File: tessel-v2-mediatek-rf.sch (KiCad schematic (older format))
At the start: 0 parts

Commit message: rf chain done (*starts praying*)
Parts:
- added AE? (x2): ANTENNA, symbol ANTENNA
- added AE? (x2): UFL, symbol UFL
- added C? (x4): 2.2pF, symbol C
- added C? (x4): 100pF, symbol C
- added C? (x2): 0.8pF, symbol C
- added C? (x4): 1.2pF, symbol C
- added C? (x4): 1.8pF, symbol C
- added L? (x4): 3nH, symbol INDUCTOR
- added L? (x4): 2.7nH, symbol INDUCTOR
- added L? (x2): 2.4nH, symbol INDUCTOR
- added R? (x2): 0R DNP, symbol R
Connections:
- net labels added: GND, RF0_BALUN_IN, RF0_CHIP_ANT, RF0_OUTN, RF0_OUTN_TCIN, RF0_OUTN_TCOUT, RF0_OUTP, RF0_OUTP_TCIN, RF0_OUTP_TCOUT, RF0_UFL, RF1_BALUN_IN, RF1_CHIP_ANT, RF1_OUTN, RF1_OUTN_TCIN, RF1_OUTN_TCOUT, RF1_OUTP, RF1_OUTP_TCIN, RF1_OUTP_TCOUT, RF1_UFL
- wire segments 0 -> 84

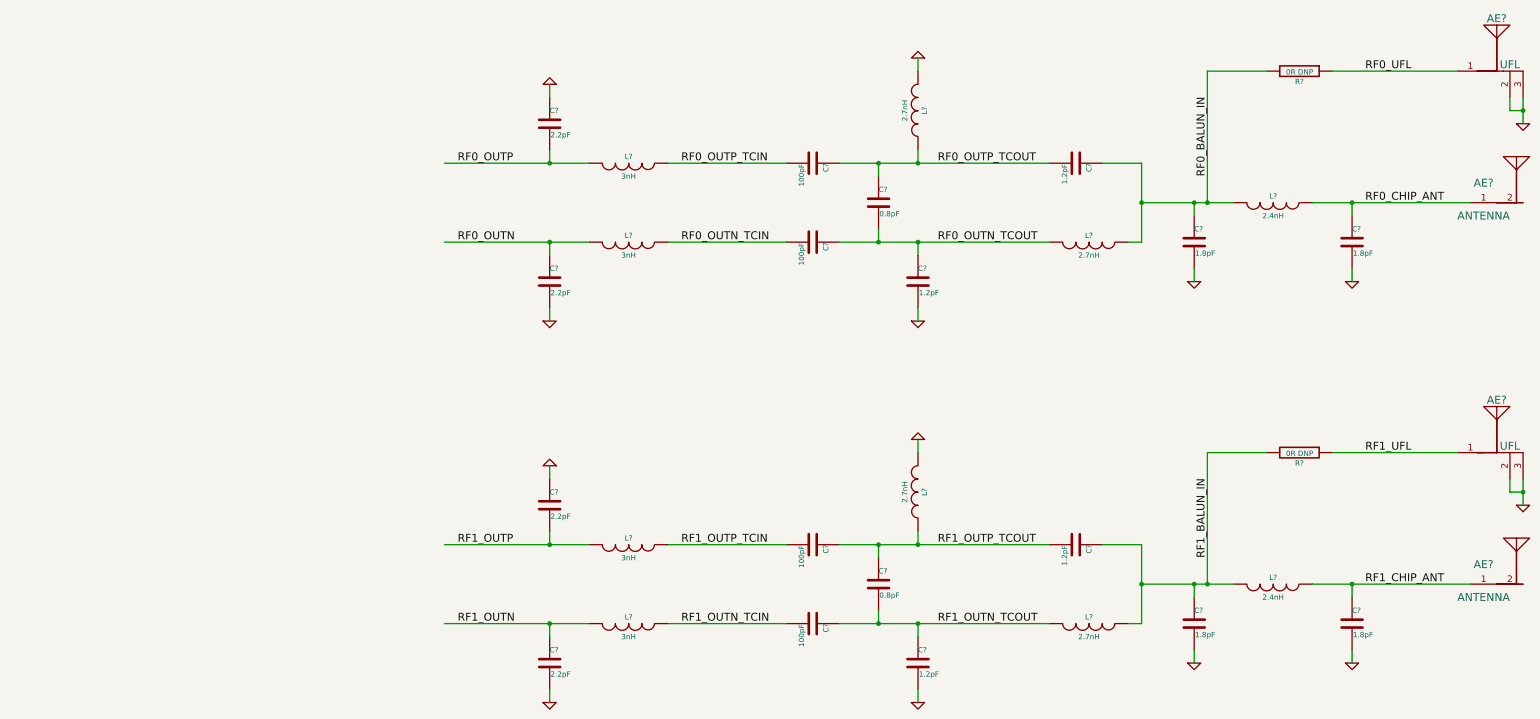
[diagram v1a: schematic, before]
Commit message: cleaning up ram, rf, and mediatek power
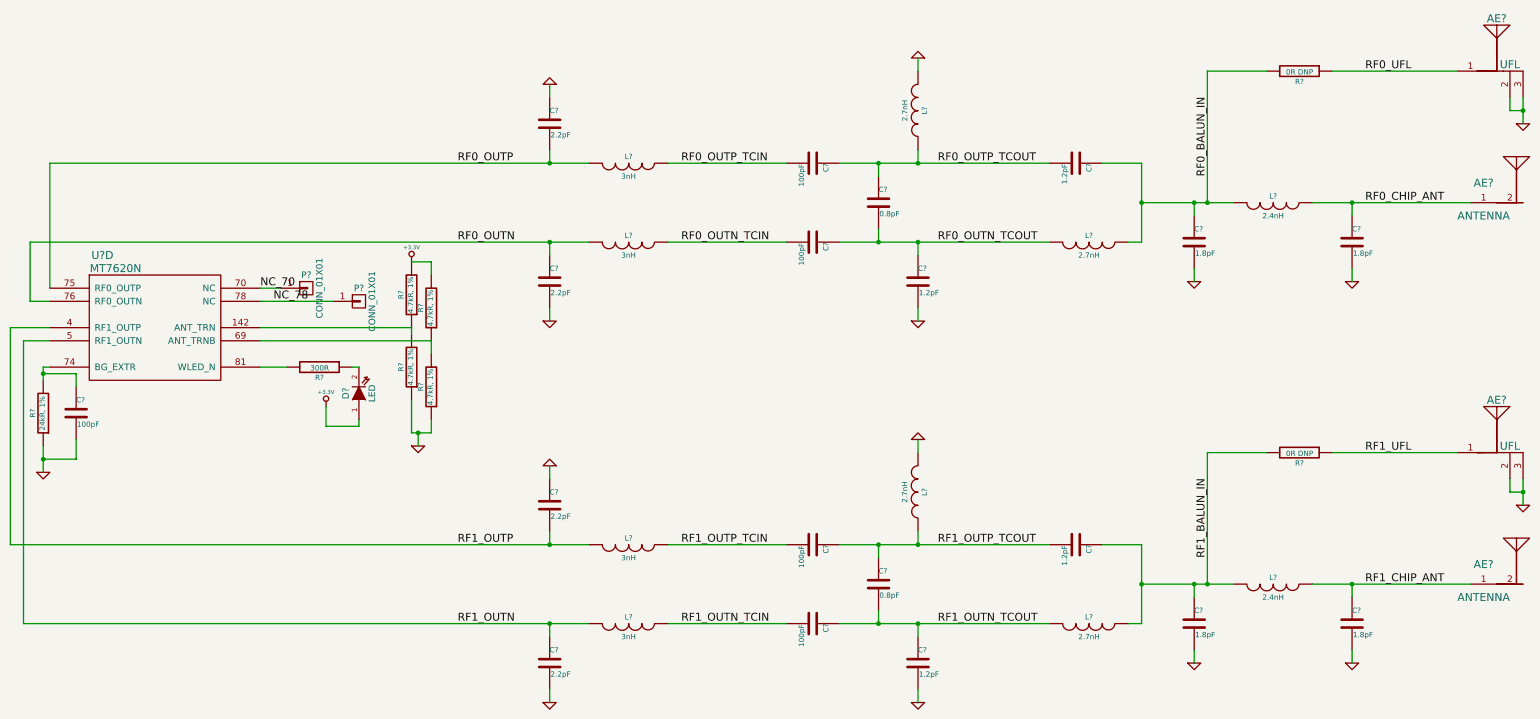
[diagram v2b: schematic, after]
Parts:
- added C?: 100pF, symbol C
- added D?: LED, symbol LED
- added P? (x2): CONN_01X01, symbol CONN_01X01
- added R?: 300R, symbol R
- added R?: 24kR, 1%, symbol R
- added R? (x4): 4.7kR, 1%, symbol R
- added U?: MT7620N, symbol MT7620N
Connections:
- net labels added: +3.3V, NC_70, NC_78
- wire segments 84 -> 93

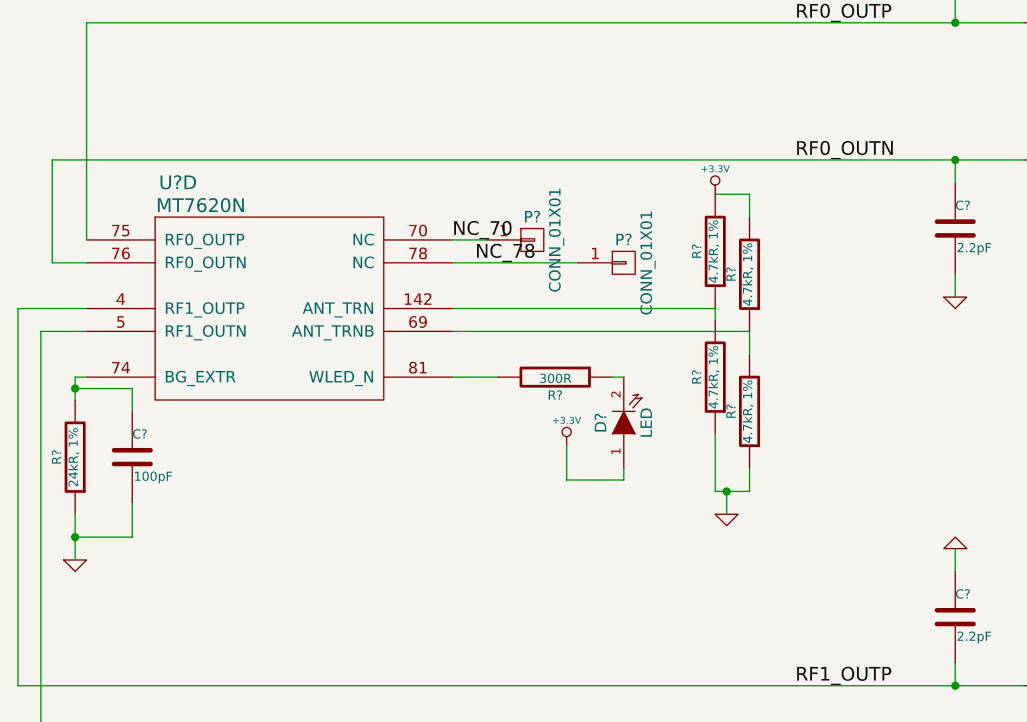
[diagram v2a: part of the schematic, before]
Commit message: setting default boot pins on rf
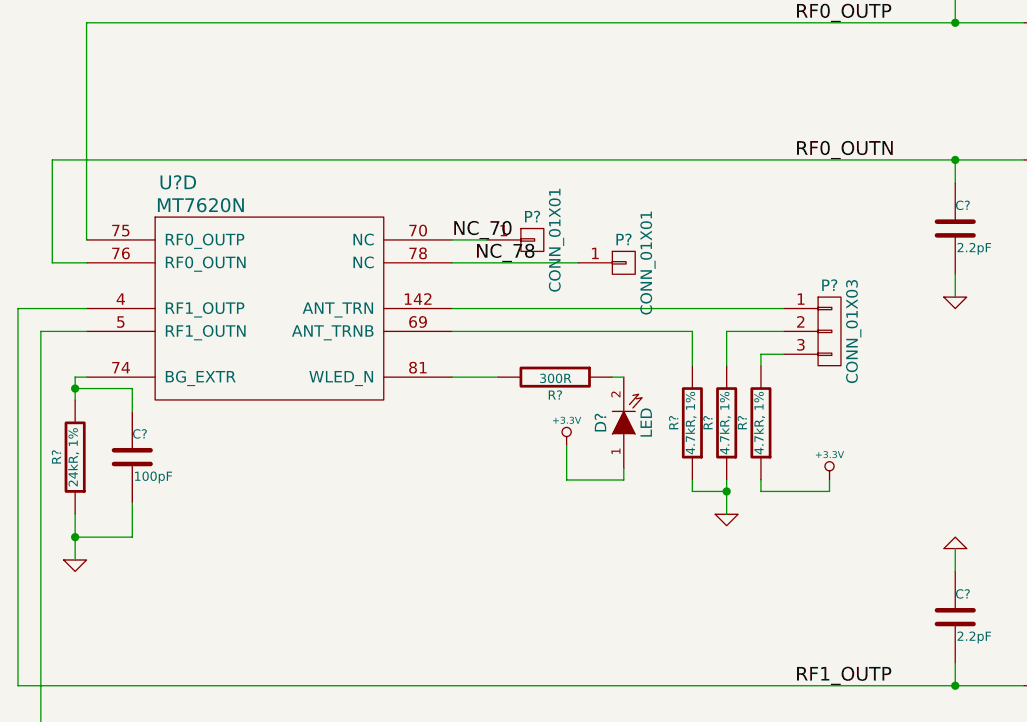
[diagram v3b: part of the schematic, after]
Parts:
- removed R?: 4.7kR, 1%, symbol R
- added P?: CONN_01X03, symbol CONN_01X03
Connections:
- net +3.3V: now also R?.1; no longer R?.2
- new net: P?.1 (P1), U?.142 (ANT_TRN)
- new net: P?.3 (P3), R?.2
- new net: P?.2 (P2), R?.2
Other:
- moved on the sheet: R?
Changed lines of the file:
@@
 	4450 5550 4450 5600
 Wire Wire Line
-	2050 5250 2050 5150
+	2050 5150 2050 5250
 Wire Wire Line
 	2050 5150 2100 5150
 Wire Wire Line
-	2050 5950 2050 5750
+	2050 5750 2050 5950
 Wire Wire Line
 	2300 5300 2300 5200
@@
 Wire Wire Line
 	4200 5600 4450 5600
-Wire Wire Line
-	3700 4850 4850 4850
 $Comp
 L R R?
 U 1 1 5491920E
-P 4850 4600
-F 0 "R?" V 4930 4600 40  0000 C CNN
-F 1 "4.7kR, 1%" V 4857 4601 40  0000 C CNN
-F 2 "" V 4780 4600 30  0000 C CNN
-F 3 "" H 4850 4600 30  0000 C CNN
-	1    4850 4600
+P 5050 5350
+F 0 "R?" V 5130 5350 40  0000 C CNN
+F 1 "4.7kR, 1%" V 5057 5351 40  0000 C CNN
+F 2 "" V 4980 5350 30  0000 C CNN
+F 3 "" H 5050 5350 30  0000 C CNN
+	1    5050 5350
 	-1   0    0    1
 $EndComp
@@
 L +3.3V #PWR?
 U 1 1 54919282
-P 4850 4350
-F 0 "#PWR?" H 4850 4310 30  0001 C CNN
-F 1 "+3.3V" H 4850 4460 30  0000 C CNN
-F 2 "" H 4850 4350 60  0000 C CNN
-F 3 "" H 4850 4350 60  0000 C CNN
-	1    4850 4350
+P 5350 5600
+F 0 "#PWR?" H 5350 5560 30  0001 C CNN
+F 1 "+3.3V" H 5350 5710 30  0000 C CNN
+F 2 "" H 5350 5600 60  0000 C CNN
+F 3 "" H 5350 5600 60  0000 C CNN
+	1    5350 5600
 	1    0    0    -1
 $EndComp
@@
 L R R?
 U 1 1 5491938E
-P 4850 5150
-F 0 "R?" V 4930 5150 40  0000 C CNN
-F 1 "4.7kR, 1%" V 4857 5151 40  0000 C CNN
-F 2 "" V 4780 5150 30  0000 C CNN
-F 3 "" H 4850 5150 30  0000 C CNN
-	1    4850 5150
+P 4900 5350
+F 0 "R?" V 4980 5350 40  0000 C CNN
+F 1 "4.7kR, 1%" V 4907 5351 40  0000 C CNN
+F 2 "" V 4830 5350 30  0000 C CNN
+F 3 "" H 4900 5350 30  0000 C CNN
+	1    4900 5350
 	-1   0    0    1
 $EndComp
@@
 L R R?
 U 1 1 54919448
-P 5000 5300
-F 0 "R?" V 5080 5300 40  0000 C CNN
-F 1 "4.7kR, 1%" V 5007 5301 40  0000 C CNN
-F 2 "" V 4930 5300 30  0000 C CNN
-F 3 "" H 5000 5300 30  0000 C CNN
-	1    5000 5300
-	-1   0    0    1
-$EndComp
-$Comp
-L R R?
-U 1 1 54919496
-P 5000 4700
-F 0 "R?" V 5080 4700 40  0000 C CNN
-F 1 "4.7kR, 1%" V 5007 4701 40  0000 C CNN
-F 2 "" V 4930 4700 30  0000 C CNN
-F 3 "" H 5000 4700 30  0000 C CNN
-	1    5000 4700
+P 4750 5350
+F 0 "R?" V 4830 5350 40  0000 C CNN
+F 1 "4.7kR, 1%" V 4757 5351 40  0000 C CNN
+F 2 "" V 4680 5350 30  0000 C CNN
+F 3 "" H 4750 5350 30  0000 C CNN
+	1    4750 5350
 	-1   0    0    1
 $EndComp
 Wire Wire Line
-	3700 4950 5000 4950
+	3700 4950 4750 4950
 Wire Wire Line
-	4850 4850 4850 4900
+	4750 4950 4750 5100
 Wire Wire Line
-	5000 4950 5000 5050
+	4750 5650 4750 5600
 Wire Wire Line
-	4850 5400 4850 5650
+	4900 5600 4900 5750
+Connection ~ 4900 5650
+$Comp
+L CONN_01X03 P?
+U 1 1 5491EAD6
+P 5350 4950
+F 0 "P?" H 5350 5150 50  0000 C CNN
+F 1 "CONN_01X03" V 5450 4950 50  0000 C CNN
+F 2 "" H 5350 4950 60  0000 C CNN
+F 3 "" H 5350 4950 60  0000 C CNN
+	1    5350 4950
+	1    0    0    -1
+$EndComp
 Wire Wire Line
-	4850 5650 5000 5650
+	3700 4850 5150 4850
 Wire Wire Line
-	5000 5650 5000 5550
+	5150 4950 4900 4950
 Wire Wire Line
-	4900 5650 4900 5750
-Connection ~ 4900 5650
+	4900 4950 4900 5100
 Wire Wire Line
-	5000 4450 5000 4350
+	4900 5650 4750 5650
 Wire Wire Line
-	5000 4350 4850 4350
+	5050 5600 5050 5650
+Wire Wire Line
+	5050 5650 5350 5650
+Wire Wire Line
+	5350 5650 5350 5600
+Wire Wire Line
+	5050 5100 5050 5050
+Wire Wire Line
+	5050 5050 5150 5050
 $EndSCHEMATC

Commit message: annotated
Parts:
- gave numbers to parts that had none: 45

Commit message: second pass schem check
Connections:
- net at U201.142 (ANT_TRN): now also P503.2 (P2); no longer P503.1 (P1)
- net at R504.2: now also P503.1 (P1); no longer P503.2 (P2)
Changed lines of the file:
@@
 $EndComp
 Wire Wire Line
-	3700 4850 5150 4850
-Wire Wire Line
-	5150 4950 4900 4950
-Wire Wire Line
-	4900 4950 4900 5100
+	4900 4900 4900 5100
 Wire Wire Line
 	4900 5650 4750 5650
@@
 Wire Wire Line
 	5050 5050 5150 5050
+Wire Wire Line
+	3700 4850 5000 4850
+Wire Wire Line
+	5000 4850 5000 4950
+Wire Wire Line
+	5000 4950 5150 4950
+Wire Wire Line
+	4900 4900 5050 4900
+Wire Wire Line
+	5050 4900 5050 4850
+Wire Wire Line
+	5050 4850 5150 4850
 $EndSCHEMATC

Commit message: adding netlist, checked for single-pin nets
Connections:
- no-connect marks 0 -> 2
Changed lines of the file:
@@
 $EndComp
 $Comp
-L GND #PWR513
+L GND #PWR027
 U 1 1 5492119C
 P 10800 4500
-F 0 "#PWR513" H 10800 4500 30  0001 C CNN
+F 0 "#PWR027" H 10800 4500 30  0001 C CNN
 F 1 "GND" H 10800 4430 30  0001 C CNN
 F 2 "" H 10800 4500 60  0000 C CNN
@@
 $EndComp
 $Comp
-L GND #PWR515
+L GND #PWR028
 U 1 1 549211F2
 P 12000 4500
-F 0 "#PWR515" H 12000 4500 30  0001 C CNN
+F 0 "#PWR028" H 12000 4500 30  0001 C CNN
 F 1 "GND" H 12000 4430 30  0001 C CNN
 F 2 "" H 12000 4500 60  0000 C CNN
@@
 $EndComp
 $Comp
-L GND #PWR517
+L GND #PWR029
 U 1 1 54921339
 P 13300 3300
-F 0 "#PWR517" H 13300 3300 30  0001 C CNN
+F 0 "#PWR029" H 13300 3300 30  0001 C CNN
 F 1 "GND" H 13300 3230 30  0001 C CNN
 F 2 "" H 13300 3300 60  0000 C CNN
@@
 $EndComp
 $Comp
-L GND #PWR510
+L GND #PWR030
 U 1 1 54921901
 P 8700 4800
-F 0 "#PWR510" H 8700 4800 30  0001 C CNN
+F 0 "#PWR030" H 8700 4800 30  0001 C CNN
 F 1 "GND" H 8700 4730 30  0001 C CNN
 F 2 "" H 8700 4800 60  0000 C CNN
@@
 $EndComp
 $Comp
-L GND #PWR506
+L GND #PWR031
 U 1 1 54921B0A
 P 5900 4800
-F 0 "#PWR506" H 5900 4800 30  0001 C CNN
+F 0 "#PWR031" H 5900 4800 30  0001 C CNN
 F 1 "GND" H 5900 4730 30  0001 C CNN
 F 2 "" H 5900 4800 60  0000 C CNN
@@
 $EndComp
 $Comp
-L GND #PWR505
+L GND #PWR032
 U 1 1 54921B48
 P 5900 3000
-F 0 "#PWR505" H 5900 3000 30  0001 C CNN
+F 0 "#PWR032" H 5900 3000 30  0001 C CNN
 F 1 "GND" H 5900 2930 30  0001 C CNN
 F 2 "" H 5900 3000 60  0000 C CNN
@@
 $EndComp
 $Comp
-L GND #PWR509
+L GND #PWR033
 U 1 1 54921BCA
 P 8700 2800
-F 0 "#PWR509" H 8700 2800 30  0001 C CNN
+F 0 "#PWR033" H 8700 2800 30  0001 C CNN
 F 1 "GND" H 8700 2730 30  0001 C CNN
 F 2 "" H 8700 2800 60  0000 C CNN
@@
 $EndComp
 $Comp
-L GND #PWR514
+L GND #PWR034
 U 1 1 5492F3B9
 P 10800 7400
-F 0 "#PWR514" H 10800 7400 30  0001 C CNN
+F 0 "#PWR034" H 10800 7400 30  0001 C CNN
 F 1 "GND" H 10800 7330 30  0001 C CNN
 F 2 "" H 10800 7400 60  0000 C CNN
@@
 $EndComp
 $Comp
-L GND #PWR516
+L GND #PWR035
 U 1 1 5492F3BF
 P 12000 7400
-F 0 "#PWR516" H 12000 7400 30  0001 C CNN
+F 0 "#PWR035" H 12000 7400 30  0001 C CNN
 F 1 "GND" H 12000 7330 30  0001 C CNN
 F 2 "" H 12000 7400 60  0000 C CNN
@@
 $EndComp
 $Comp
-L GND #PWR518
+L GND #PWR036
 U 1 1 5492F3C5
 P 13300 6200
-F 0 "#PWR518" H 13300 6200 30  0001 C CNN
+F 0 "#PWR036" H 13300 6200 30  0001 C CNN
 F 1 "GND" H 13300 6130 30  0001 C CNN
 F 2 "" H 13300 6200 60  0000 C CNN
@@
 $EndComp
 $Comp
-L GND #PWR512
+L GND #PWR037
 U 1 1 5492F3D0
 P 8700 7700
-F 0 "#PWR512" H 8700 7700 30  0001 C CNN
+F 0 "#PWR037" H 8700 7700 30  0001 C CNN
 F 1 "GND" H 8700 7630 30  0001 C CNN
 F 2 "" H 8700 7700 60  0000 C CNN
@@
 $EndComp
 $Comp
-L GND #PWR508
+L GND #PWR038
 U 1 1 5492F3D6
 P 5900 7700
-F 0 "#PWR508" H 5900 7700 30  0001 C CNN
+F 0 "#PWR038" H 5900 7700 30  0001 C CNN
 F 1 "GND" H 5900 7630 30  0001 C CNN
 F 2 "" H 5900 7700 60  0000 C CNN
@@
 $EndComp
 $Comp
-L GND #PWR507
+L GND #PWR039
 U 1 1 5492F3DC
 P 5900 5900
-F 0 "#PWR507" H 5900 5900 30  0001 C CNN
+F 0 "#PWR039" H 5900 5900 30  0001 C CNN
 F 1 "GND" H 5900 5830 30  0001 C CNN
 F 2 "" H 5900 5900 60  0000 C CNN
@@
 $EndComp
 $Comp
-L GND #PWR511
+L GND #PWR040
 U 1 1 5492F3E2
 P 8700 5700
-F 0 "#PWR511" H 8700 5700 30  0001 C CNN
+F 0 "#PWR040" H 8700 5700 30  0001 C CNN
 F 1 "GND" H 8700 5630 30  0001 C CNN
 F 2 "" H 8700 5700 60  0000 C CNN
@@
 $EndComp
 $Comp
-L +3.3V #PWR502
+L +3.3V #PWR041
 U 1 1 54916FFB
 P 4200 5450
-F 0 "#PWR502" H 4200 5410 30  0001 C CNN
+F 0 "#PWR041" H 4200 5410 30  0001 C CNN
 F 1 "+3.3V" H 4200 5560 30  0000 C CNN
 F 2 "" H 4200 5450 60  0000 C CNN
@@
 $EndComp
 $Comp
-L GND #PWR501
+L GND #PWR042
 U 1 1 54917BEF
 P 2050 5950
-F 0 "#PWR501" H 2050 5950 30  0001 C CNN
+F 0 "#PWR042" H 2050 5950 30  0001 C CNN
 F 1 "GND" H 2050 5880 30  0001 C CNN
 F 2 "" H 2050 5950 60  0000 C CNN
@@
 NC_78
 $Comp
-L GND #PWR503
+L GND #PWR043
 U 1 1 54918F7B
 P 4900 5750
-F 0 "#PWR503" H 4900 5750 30  0001 C CNN
+F 0 "#PWR043" H 4900 5750 30  0001 C CNN
 F 1 "GND" H 4900 5680 30  0001 C CNN
 F 2 "" H 4900 5750 60  0000 C CNN
@@
 $EndComp
 $Comp
-L +3.3V #PWR504
+L +3.3V #PWR044
 U 1 1 54919282
 P 5350 5600
-F 0 "#PWR504" H 5350 5560 30  0001 C CNN
+F 0 "#PWR044" H 5350 5560 30  0001 C CNN
 F 1 "+3.3V" H 5350 5710 30  0000 C CNN
 F 2 "" H 5350 5600 60  0000 C CNN
@@
 Wire Wire Line
 	5050 4850 5150 4850
+NoConn ~ 13300 3900
+NoConn ~ 13300 6800
 $EndSCHEMATC

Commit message: TIL: -am...but also P-->J
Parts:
- renumbered P501 to J501, P502 to J502, P503 to J503
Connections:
- net ANT_TRN: now reaches J503.2 (P2), U201.142 (ANT_TRN)
- net ANT_TRNB: now reaches R503.2, U201.69 (ANT_TRNB)
- net WLED_N: now reaches R502.2, U201.81 (WLED_N)
- net WLED_N_R: now reaches D501.2 (K), R502.1
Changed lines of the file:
@@
 $EndComp
 $Comp
-L GND #PWR027
+L GND #PWR513
 U 1 1 5492119C
 P 10800 4500
-F 0 "#PWR027" H 10800 4500 30  0001 C CNN
+F 0 "#PWR513" H 10800 4500 30  0001 C CNN
 F 1 "GND" H 10800 4430 30  0001 C CNN
 F 2 "" H 10800 4500 60  0000 C CNN
@@
 $EndComp
 $Comp
-L GND #PWR028
+L GND #PWR515
 U 1 1 549211F2
 P 12000 4500
-F 0 "#PWR028" H 12000 4500 30  0001 C CNN
+F 0 "#PWR515" H 12000 4500 30  0001 C CNN
 F 1 "GND" H 12000 4430 30  0001 C CNN
 F 2 "" H 12000 4500 60  0000 C CNN
@@
 $EndComp
 $Comp
-L GND #PWR029
+L GND #PWR517
 U 1 1 54921339
 P 13300 3300
-F 0 "#PWR029" H 13300 3300 30  0001 C CNN
+F 0 "#PWR517" H 13300 3300 30  0001 C CNN
 F 1 "GND" H 13300 3230 30  0001 C CNN
 F 2 "" H 13300 3300 60  0000 C CNN
@@
 $EndComp
 $Comp
-L GND #PWR030
+L GND #PWR510
 U 1 1 54921901
 P 8700 4800
-F 0 "#PWR030" H 8700 4800 30  0001 C CNN
+F 0 "#PWR510" H 8700 4800 30  0001 C CNN
 F 1 "GND" H 8700 4730 30  0001 C CNN
 F 2 "" H 8700 4800 60  0000 C CNN
@@
 $EndComp
 $Comp
-L GND #PWR031
+L GND #PWR506
 U 1 1 54921B0A
 P 5900 4800
-F 0 "#PWR031" H 5900 4800 30  0001 C CNN
+F 0 "#PWR506" H 5900 4800 30  0001 C CNN
 F 1 "GND" H 5900 4730 30  0001 C CNN
 F 2 "" H 5900 4800 60  0000 C CNN
@@
 $EndComp
 $Comp
-L GND #PWR032
+L GND #PWR505
 U 1 1 54921B48
 P 5900 3000
-F 0 "#PWR032" H 5900 3000 30  0001 C CNN
+F 0 "#PWR505" H 5900 3000 30  0001 C CNN
 F 1 "GND" H 5900 2930 30  0001 C CNN
 F 2 "" H 5900 3000 60  0000 C CNN
@@
 $EndComp
 $Comp
-L GND #PWR033
+L GND #PWR509
 U 1 1 54921BCA
 P 8700 2800
-F 0 "#PWR033" H 8700 2800 30  0001 C CNN
+F 0 "#PWR509" H 8700 2800 30  0001 C CNN
 F 1 "GND" H 8700 2730 30  0001 C CNN
 F 2 "" H 8700 2800 60  0000 C CNN
@@
 $EndComp
 $Comp
-L GND #PWR034
+L GND #PWR514
 U 1 1 5492F3B9
 P 10800 7400
-F 0 "#PWR034" H 10800 7400 30  0001 C CNN
+F 0 "#PWR514" H 10800 7400 30  0001 C CNN
 F 1 "GND" H 10800 7330 30  0001 C CNN
 F 2 "" H 10800 7400 60  0000 C CNN
@@
 $EndComp
 $Comp
-L GND #PWR035
+L GND #PWR516
 U 1 1 5492F3BF
 P 12000 7400
-F 0 "#PWR035" H 12000 7400 30  0001 C CNN
+F 0 "#PWR516" H 12000 7400 30  0001 C CNN
 F 1 "GND" H 12000 7330 30  0001 C CNN
 F 2 "" H 12000 7400 60  0000 C CNN
@@
 $EndComp
 $Comp
-L GND #PWR036
+L GND #PWR518
 U 1 1 5492F3C5
 P 13300 6200
-F 0 "#PWR036" H 13300 6200 30  0001 C CNN
+F 0 "#PWR518" H 13300 6200 30  0001 C CNN
 F 1 "GND" H 13300 6130 30  0001 C CNN
 F 2 "" H 13300 6200 60  0000 C CNN
@@
 $EndComp
 $Comp
-L GND #PWR037
+L GND #PWR512
 U 1 1 5492F3D0
 P 8700 7700
-F 0 "#PWR037" H 8700 7700 30  0001 C CNN
+F 0 "#PWR512" H 8700 7700 30  0001 C CNN
 F 1 "GND" H 8700 7630 30  0001 C CNN
 F 2 "" H 8700 7700 60  0000 C CNN
@@
 $EndComp
 $Comp
-L GND #PWR038
+L GND #PWR508
 U 1 1 5492F3D6
 P 5900 7700
-F 0 "#PWR038" H 5900 7700 30  0001 C CNN
+F 0 "#PWR508" H 5900 7700 30  0001 C CNN
 F 1 "GND" H 5900 7630 30  0001 C CNN
 F 2 "" H 5900 7700 60  0000 C CNN
@@
 $EndComp
 $Comp
-L GND #PWR039
+L GND #PWR507
 U 1 1 5492F3DC
 P 5900 5900
-F 0 "#PWR039" H 5900 5900 30  0001 C CNN
+F 0 "#PWR507" H 5900 5900 30  0001 C CNN
 F 1 "GND" H 5900 5830 30  0001 C CNN
 F 2 "" H 5900 5900 60  0000 C CNN
@@
 $EndComp
 $Comp
-L GND #PWR040
+L GND #PWR511
 U 1 1 5492F3E2
 P 8700 5700
-F 0 "#PWR040" H 8700 5700 30  0001 C CNN
+F 0 "#PWR511" H 8700 5700 30  0001 C CNN
 F 1 "GND" H 8700 5630 30  0001 C CNN
 F 2 "" H 8700 5700 60  0000 C CNN
@@
 $EndComp
 $Comp
-L +3.3V #PWR041
+L +3.3V #PWR502
 U 1 1 54916FFB
 P 4200 5450
-F 0 "#PWR041" H 4200 5410 30  0001 C CNN
+F 0 "#PWR502" H 4200 5410 30  0001 C CNN
 F 1 "+3.3V" H 4200 5560 30  0000 C CNN
 F 2 "" H 4200 5450 60  0000 C CNN
@@
 $EndComp
 $Comp
-L GND #PWR042
+L GND #PWR501
 U 1 1 54917BEF
 P 2050 5950
-F 0 "#PWR042" H 2050 5950 30  0001 C CNN
+F 0 "#PWR501" H 2050 5950 30  0001 C CNN
 F 1 "GND" H 2050 5880 30  0001 C CNN
 F 2 "" H 2050 5950 60  0000 C CNN
@@
 Connection ~ 2050 5850
 $Comp
-L CONN_01X01 P501
+L CONN_01X01 J501
 U 1 1 54918BC9
 P 4050 4550
-F 0 "P501" H 4050 4650 50  0000 C CNN
+F 0 "J501" H 4050 4650 50  0000 C CNN
 F 1 "CONN_01X01" V 4150 4550 50  0000 C CNN
 F 2 "" H 4050 4550 60  0000 C CNN
@@
 $EndComp
 $Comp
-L CONN_01X01 P502
+L CONN_01X01 J502
 U 1 1 54918C42
 P 4450 4650
-F 0 "P502" H 4450 4750 50  0000 C CNN
+F 0 "J502" H 4450 4750 50  0000 C CNN
 F 1 "CONN_01X01" V 4550 4650 50  0000 C CNN
 F 2 "" H 4450 4650 60  0000 C CNN
@@
 NC_78
 $Comp
-L GND #PWR043
+L GND #PWR503
 U 1 1 54918F7B
 P 4900 5750
-F 0 "#PWR043" H 4900 5750 30  0001 C CNN
+F 0 "#PWR503" H 4900 5750 30  0001 C CNN
 F 1 "GND" H 4900 5680 30  0001 C CNN
 F 2 "" H 4900 5750 60  0000 C CNN
@@
 $EndComp
 $Comp
-L +3.3V #PWR044
+L +3.3V #PWR504
 U 1 1 54919282
 P 5350 5600
-F 0 "#PWR044" H 5350 5560 30  0001 C CNN
+F 0 "#PWR504" H 5350 5560 30  0001 C CNN
 F 1 "+3.3V" H 5350 5710 30  0000 C CNN
 F 2 "" H 5350 5600 60  0000 C CNN
@@
 Connection ~ 4900 5650
 $Comp
-L CONN_01X03 P503
+L CONN_01X03 J503
 U 1 1 5491EAD6
 P 5350 4950
-F 0 "P503" H 5350 5150 50  0000 C CNN
+F 0 "J503" H 5350 5150 50  0000 C CNN
 F 1 "CONN_01X03" V 5450 4950 50  0000 C CNN
 F 2 "" H 5350 4950 60  0000 C CNN
@@
 NoConn ~ 13300 3900
 NoConn ~ 13300 6800
+Text Label 3750 4850 0    60   ~ 0
+ANT_TRN
+Text Label 3750 4950 0    60   ~ 0
+ANT_TRNB
+Text Label 3750 5150 0    60   ~ 0
+WLED_N
+Text Label 4400 5150 0    60   ~ 0
+WLED_N_R
 $EndSCHEMATC
